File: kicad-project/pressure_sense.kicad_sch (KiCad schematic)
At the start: 27 parts

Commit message: cleaning up footprints
used easyeda2kicad.py to get better footprints (with 3d models) (https://github.com/uPesy/easyeda2kicad.py)

it's kinda messy bc some symbols are kicad and others easyeda, shouldn't matter tho (e.g. on C6 can't see the 470u value, only part ref)
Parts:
- removed C6: 470u, 470uF:CAP-SMD_BD6.3-L6.6-W6.6-FD, symbol Device:C_Polarized
- removed H1: X6521WR-2×17H-C30D60, 2*17P:HDR-TH_34P-P2.54-H-M-R2-C17-S2.54, symbol 2*17P:X6521WR-2×17H-C30D60
- removed JL1, JR1: Conn_01x22_Socket, 22P:HDR-TH_22P-P2.54-V-M, symbol Connector:Conn_01x22_Socket
- removed JPWR1: Screw_Terminal_01x02, 2P:CONN-TH_P2.54_KF128-2.54-2P, symbol Connector:Screw_Terminal_01x02
- removed RV1: 20k, pot:RES-ADJ-TH_3P-L7.1-W6.9-P2.50-L_3362P, symbol Device:R_Potentiometer_Trim
- removed UA1, UB1: SN74HC163DR_C338758, SN74HC163DR:SOIC-16_L9.9-W3.9-P1.27-LS6.0-BL, symbol SN74HC163DR:SN74HC163DR_C338758
- removed UA2, UB2: CD74HC4067SM96, CD74HC4067SM96:SSOP-24_L8.1-W5.3-P0.65-LS7.8-BL, symbol CD74HC6946SM96:CD74HC4067SM96
- removed USBC1: TYPE-C-31-M-12, USBC:USB-C_SMD-TYPE-C-31-M-12_1, symbol USBC:TYPE-C-31-M-12
- added C6: UT1A471M0607VG, easyeda2kicad:CAP-SMD_BD6.3-L6.6-W6.6-FD, symbol easyeda2kicad:UT1A471M0607VG
- added H2, H3, H4: MountingHole, MountingHole:MountingHole_3.2mm_M3, symbol Mechanical:MountingHole
- added H5: X6521WR-2×17H-C30D60, easyeda2kicad:HDR-TH_34P-P2.54-H-M-R2-C17-S2.54, symbol easyeda2kicad:X6521WR-2×17H-C30D60
- added JL1, JR1: FH2.54-09-22PZD, easyeda2kicad:HDR-TH_22P-P2.54-V-M, symbol easyeda2kicad:FH2.54-09-22PZD
- added JPWR1: KF128-2.54-2P, easyeda2kicad:CONN-TH_P2.54_KF128-2.54-2P, symbol easyeda2kicad:KF128-2.54-2P
- added RV1: 3362P-1-203_C118933, easyeda2kicad:RES-ADJ-TH_3P-L7.1-W6.9-P2.50-L_3362P, symbol easyeda2kicad:3362P-1-203_C118933
- added UA1, UB1: SN74HC163DR_C338758, easyeda2kicad:SOIC-16_L9.9-W3.9-P1.27-LS6.0-BL, symbol easyeda2kicad:SN74HC163DR_C338758
- added UA2, UB2: CD74HC4067SM96, easyeda2kicad:SSOP-24_L8.1-W5.3-P0.65-LS7.8-BL, symbol easyeda2kicad:CD74HC4067SM96
- added USBC1: TYPE-C-31-M-12, easyeda2kicad:USB-C_SMD-TYPE-C-31-M-12_1, symbol easyeda2kicad:TYPE-C-31-M-12
- C1, C10, C2, C3, C7, C9: footprint 100nF:C0402 -> easyeda2kicad:C0402
- C4: footprint 100nF:C0402 -> easyeda2kicad:C0402; JLC_3DModel 32fe2cf9314f444ca2785a33c2db7189 -> (none); JLC_3D_Size 1 0.5 -> (none)
- C5: footprint 1000uF:CAP-SMD_BD10.0-L10.3-W10.3-LS11.3-FD -> easyeda2kicad:CAP-SMD_BD10.0-L10.3-W10.3-FD
- JA1, JB1: footprint IDC:IDC-TH_16P-P2.54_C3406 -> easyeda2kicad:IDC-TH_16P-P2.54_C3406
- JLED1: footprint 3P:CONN-TH_3P-P2.54_KF128-2.54-3P -> easyeda2kicad:CONN-TH_3P-P2.54_KF128-2.54-3P
- LED1: footprint _WS2812B-2020-V6:LED-SMD_4P-L2.2-W2.0-P1.00_WS2815C-2020-4P -> easyeda2kicad:LED-SMD_4P-L2.2-W2.0-P1.00_WS2815C-2020-4P
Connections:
- net +3.3V: now also H5.33, JL1.1, JL1.2, UA1.10 (ENT), UA1.16 (VCC), UA1.7 (ENP), UA1.9 (~{LOAD}), UA2.24 (VCC), UB1.10 (ENT), UB1.16 (VCC), UB1.9 (~{LOAD}), UB2.24 (VCC)
- net +5V: now also C4.2, C6.1, JL1.21, JPWR1.1, USBC1.A4B9 (VBUS), USBC1.B4A9 (VBUS); no longer C4.1
- net D0: now also H5.7, JR1.14
- net D1: now also H5.27, JR1.4
- net D10: now also H5.16, JL1.16
- net D11: now also H5.14, JL1.17
- net D12: now also H5.12, JL1.18
- net D13: now also H5.10, JL1.19
- net D14: now also H5.8, JL1.20
- net D15: now also H5.32, JL1.8
- net D16: now also H5.30, JL1.9
- net D17: now also H5.28, JL1.10
- net D18: now also H5.26, JL1.11
- net D19: now also H5.1, JR1.20
- net D2: now also H5.25, JR1.5
- net D20: now also H5.2, JR1.19
- net D21: now also H5.4, JR1.18
- net D3: now also H5.22, JL1.13
- net D35: now also H5.9, JR1.13
- net D36: now also H5.11, JR1.12
- net D37: now also H5.13, JR1.11
- net D38: now also H5.15, JR1.10
- net D39: now also H5.17, JR1.9
- net D4: now also JL1.4, RV1.2, UB2.1 (COMMONINOUT/OUTPUT)
- net D40: now also H5.19, JR1.8
- net D41: now also H5.21, JR1.7
- net D42: now also H5.23, JR1.6
- net D45: now also H5.5, JR1.15
- net D46: now also H5.20, JL1.14
- net D47: now also H5.6, JR1.17
- net D48: now also H5.3, JR1.16
- net D5: now also JL1.5
- net D6: now also JL1.6, UA1.2 (CLK), UB1.2 (CLK)
- net D7: now also JL1.7, UA1.1 (~{CLR}), UB1.1 (~{CLR})
- net D8: now also H5.24, JL1.12
- net D9: now also H5.18, JL1.15
- net GND: now also C4.1, C6.2, JL1.22, JPWR1.2, JR1.1, JR1.21, JR1.22, UA1.3 (A), UA1.4 (B), UA1.5 (C), UA1.6 (D), UA1.8 (GND), UA2.1 (COMMONINOUT/OUTPUT), UA2.12 (GND), UA2.15 (~{E}), UB1.3 (A), UB1.4 (B), UB1.5 (C), UB1.6 (D), UB1.8 (GND), UB2.12 (GND), UB2.15 (~{E}), USBC1.1 (EH), USBC1.2 (EH), USBC1.3 (EH), USBC1.4 (EH), USBC1.A1B12 (GND), USBC1.B1A12 (GND); no longer C4.2
- net I0A: now also UA2.9 (I0)
- net I0B: now also UB2.9 (I0)
- net I10A: now also UA2.21 (I10)
- net I10B: now also UB2.21 (I10)
- net I11A: now also UA2.20 (I11)
- net I11B: now also UB2.20 (I11)
- net I12A: now also UA2.19 (I12)
- net I12B: now also UB2.19 (I12)
- net I13A: now also UA2.18 (I13)
- net I13B: now also UB2.18 (I13)
- net I14A: now also UA2.17 (I14)
- net I14B: now also UB2.17 (I14)
- net I15A: now also UA2.16 (I15)
- net I15B: now also UB2.16 (I15)
- net I1A: now also UA2.8 (I1)
- net I1B: now also UB2.8 (I1)
- net I2A: now also UA2.7 (I2)
- net I2B: now also UB2.7 (I2)
- net I3A: now also UA2.6 (I3)
- net I3B: now also UB2.6 (I3)
- net I4A: now also UA2.5 (I4)
- net I4B: now also UB2.5 (I4)
- net I5A: now also UA2.4 (I5)
- net I5B: now also UB2.4 (I5)
- net I6A: now also UA2.3 (I6)
- net I6B: now also UB2.3 (I6)
- net I7A: now also UA2.2 (I7)
- net I7B: now also UB2.2 (I7)
- net I8A: now also UA2.23 (I8)
- net I8B: now also UB2.23 (I8)
- net I9A: now also UA2.22 (I9)
- net I9B: now also UB2.22 (I9)
- net QA1: now also UA1.14 (QA), UA2.11 (S1)
- net QA2: now also UB1.14 (QA), UB2.11 (S1)
- net QB1: now also UA1.13 (QB), UA2.10 (S0)
- net QB2: now also UB1.13 (QB), UB2.10 (S0)
- net QC1: now also UA1.12 (QC), UA2.14 (S2)
- net QC2: now also UB1.12 (QC), UB2.14 (S2)
- net QD1: now also UA1.11 (QD), UA2.13 (S3)
- net QD2: now also UB1.11 (QD), UB2.13 (S3)
- net RCO: now also UA1.15 (RCO), UB1.7 (ENP)
- net RST: now also H5.34, JL1.3
- net RX: now also H5.29, JR1.3
- net TX: now also H5.31, JR1.2
- net at R4.2: now also RV1.3
- net at R1.1: now also USBC1.A5 (CC1)
- net at R2.2: now also USBC1.B5 (CC2)
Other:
- moved on the sheet: R4

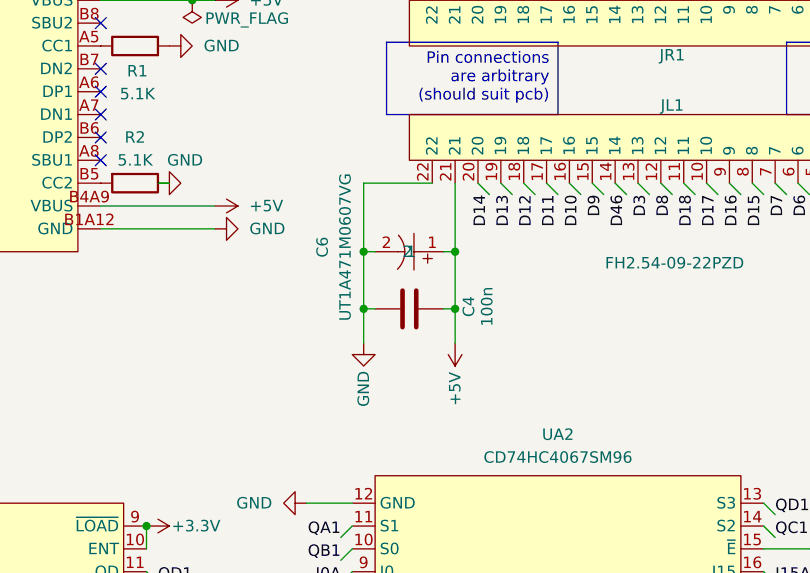
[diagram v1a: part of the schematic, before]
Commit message: changed capacitor for cost
the two smd caps cost extra $6 just for the toolhead! I changed it to one tht that is hand-soldered (the leads need to be bent)
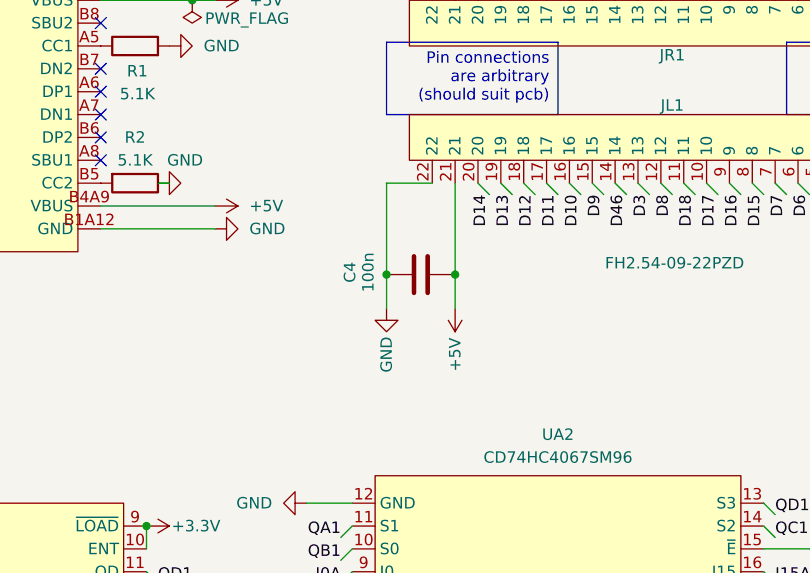
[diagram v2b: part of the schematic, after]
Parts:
- removed C6: UT1A471M0607VG, easyeda2kicad:CAP-SMD_BD6.3-L6.6-W6.6-FD, symbol easyeda2kicad:UT1A471M0607VG
- C5: footprint easyeda2kicad:CAP-SMD_BD10.0-L10.3-W10.3-FD -> easyeda2kicad:CAP-TH_BD10.0-P5.00-D0.6-FD
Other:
- moved on the sheet: C4

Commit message: changed usbc port
the port had tiny pads, i changed it for a less dodgy 6p one cause I don't need data

dw I adjusted positions.csv
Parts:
- removed USBC1: TYPE-C-31-M-12, easyeda2kicad:USB-C_SMD-TYPE-C-31-M-12_1, symbol easyeda2kicad:TYPE-C-31-M-12
- added USB1: TYPE-C 6P, easyeda2kicad:TYPE-C-SMD_TYPE-C-6P_1, symbol easyeda2kicad:TYPE-C6P
- C1, C10, C2, C3, C4, C7, C9: LCSC Part (none) -> C1525; LCSC Part # C1525 -> (none)
- C5: footprint easyeda2kicad:CAP-TH_BD10.0-P5.00-D0.6-FD -> footprints:cap_flat; LCSC Part (none) -> C439782; LCSC Part # C3359 -> (none)
- H2, H3, H4: LCSC Part (none) -> C725929
- H5: LCSC Part (none) -> C3406; LCSC Part # C725929 -> (none)
- JA1, JB1: LCSC Part (none) -> C7500786; LCSC Part # C3406 -> (none)
- JL1, JR1: LCSC Part (none) -> C474921; LCSC Part # C7500786 -> (none)
- JLED1: LCSC Part (none) -> C474920; LCSC Part # C474921 -> (none)
- JPWR1: LCSC Part (none) -> C52917434; LCSC Part # C474920 -> (none)
- LED1: LCSC Part (none) -> C25905; LCSC Part # C52917434 -> (none)
- R1, R2: LCSC Part (none) -> C25104; LCSC Part # C25905 -> (none)
- R3: LCSC Part (none) -> C25890; LCSC Part # C25104 -> (none)
- R4: LCSC Part (none) -> C118933; LCSC Part # C25890 -> (none)
- RV1: LCSC Part (none) -> C338758; LCSC Part # C118933 -> (none)
- UA1, UB1: LCSC Part (none) -> C98457; LCSC Part # C338758 -> (none)
- UA2, UB2: LCSC Part (none) -> C1525; LCSC Part # C98457 -> (none)
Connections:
- net +5V: now also USB1.A9 (VBUS), USB1.B9 (VBUS)
- net GND: now also USB1.7 (EH), USB1.A12 (GND), USB1.B12 (GND); no longer JR1.1
- net at R1.1: now also USB1.A5 (CC1)
- net at R2.2: now also USB1.B5 (CC2)
- no-connect marks 8 -> 3

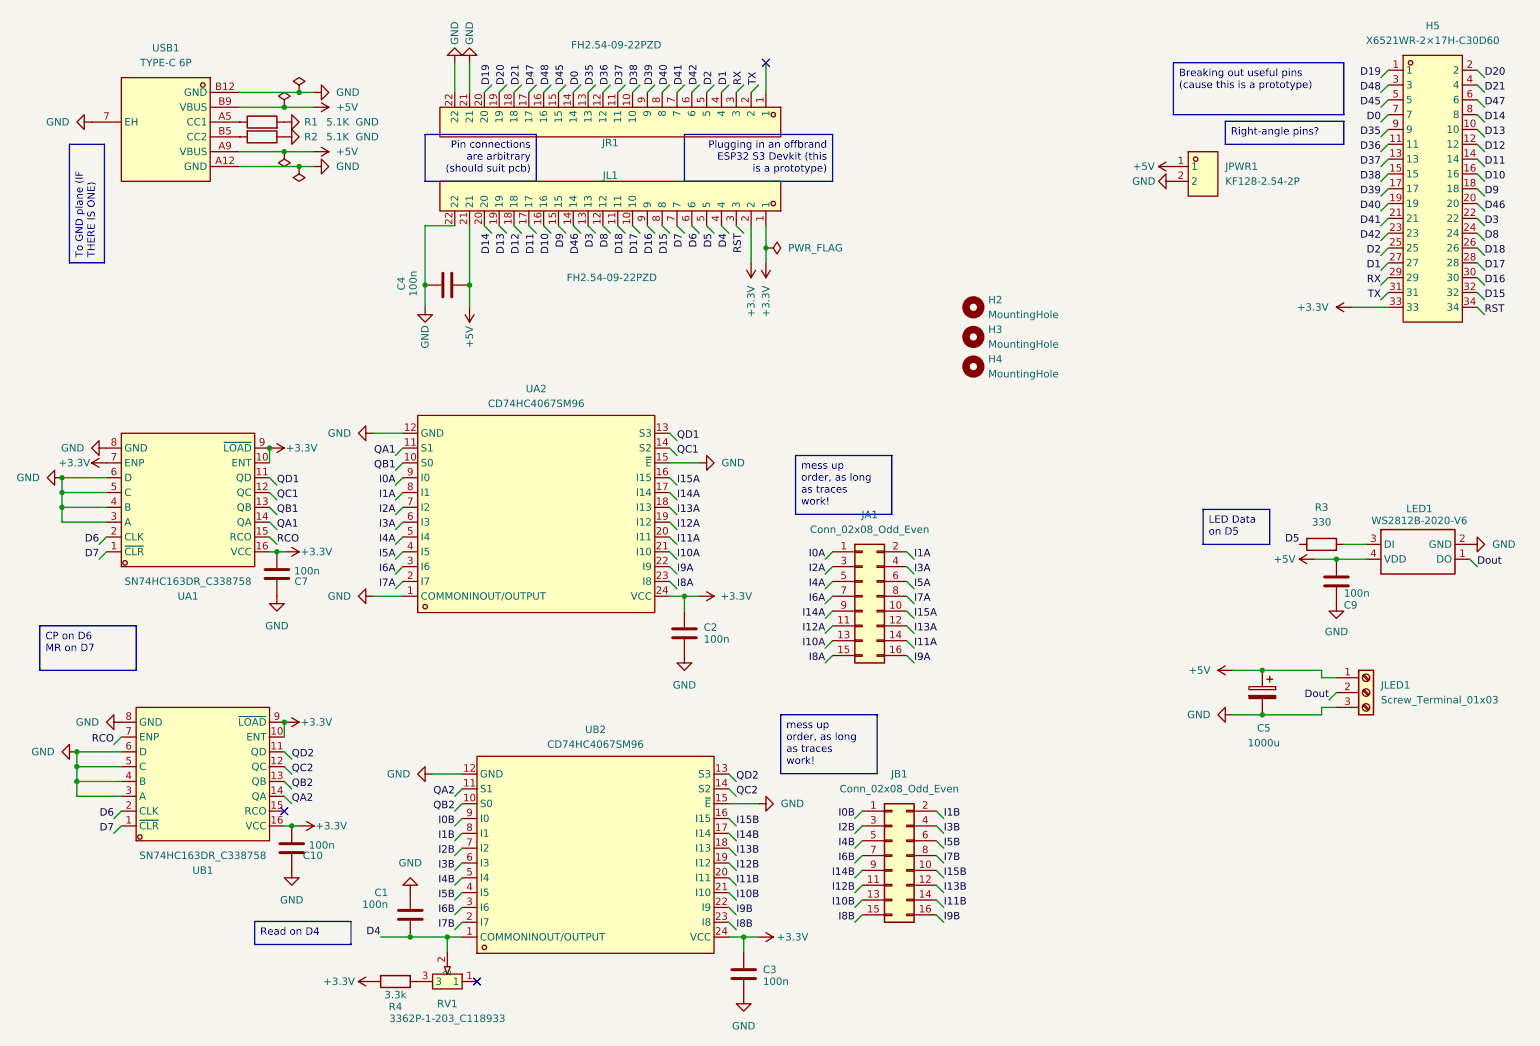
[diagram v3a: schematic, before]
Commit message: BIG CHANGE TO PCB
So since there's actually more time on Fallout, I decided to make the schematic simpler (so it's cheaper and smaller) by removing the uneccesary 74hc163 counters (there's plenty of gpio!)
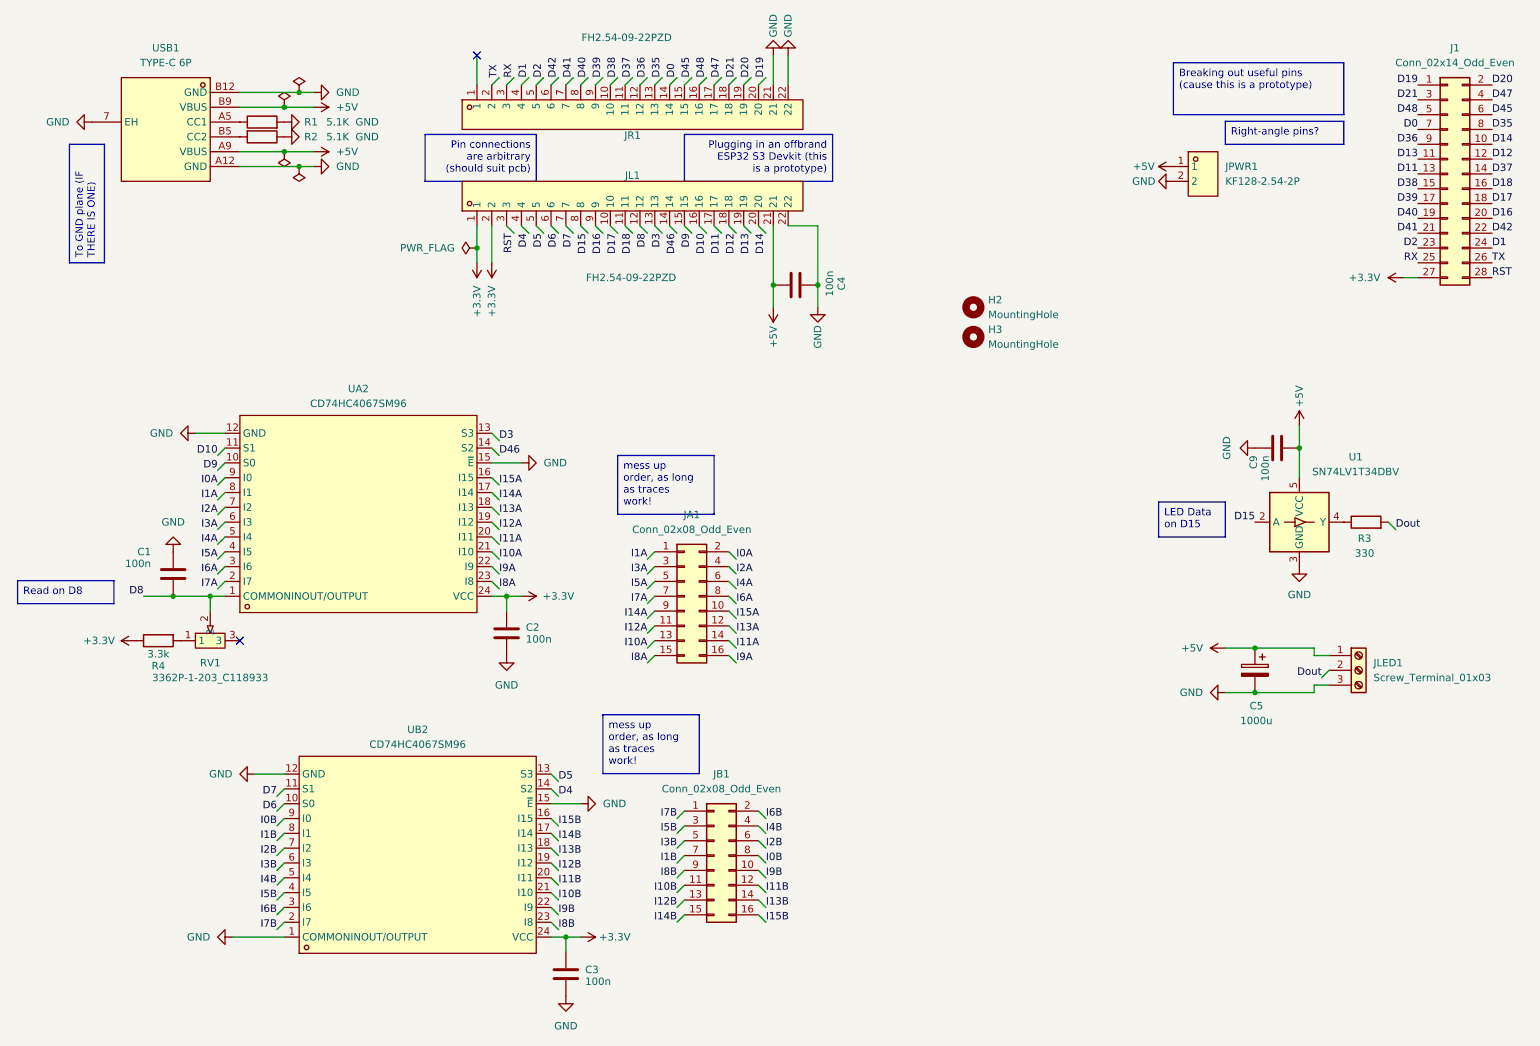
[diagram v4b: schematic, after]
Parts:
- removed C10, C7: 100n, easyeda2kicad:C0402, symbol Device:C
- removed H4: MountingHole, MountingHole:MountingHole_3.2mm_M3, symbol Mechanical:MountingHole
- removed H5: X6521WR-2×17H-C30D60, easyeda2kicad:HDR-TH_34P-P2.54-H-M-R2-C17-S2.54, symbol easyeda2kicad:X6521WR-2×17H-C30D60
- removed LED1: WS2812B-2020-V6, easyeda2kicad:LED-SMD_4P-L2.2-W2.0-P1.00_WS2815C-2020-4P, symbol _WS2812B-2020-V6:WS2812B-2020-V6
- removed UA1, UB1: SN74HC163DR_C338758, easyeda2kicad:SOIC-16_L9.9-W3.9-P1.27-LS6.0-BL, symbol easyeda2kicad:SN74HC163DR_C338758
- added J1: Conn_02x14_Odd_Even, easyeda2kicad:HDR-TH_28P-P2.54-H-M-R2-C14-S2.54, symbol Connector_Generic:Conn_02x14_Odd_Even
- added U1: SN74LV1T34DBV, Package_TO_SOT_SMD:SOT-23-5_HandSoldering, symbol Logic_LevelTranslator:SN74LV1T34DBV
- C1, C2, C3, C4, C9: footprint easyeda2kicad:C0402 -> Capacitor_SMD:C_0805_2012Metric_Pad1.18x1.45mm_HandSolder; LCSC Part C1525 -> C28233
- R1, R2: footprint Resistor_SMD:R_0402_1005Metric -> Resistor_SMD:R_0805_2012Metric_Pad1.20x1.40mm_HandSolder; LCSC Part C25104 -> C27834
- R3: footprint Resistor_SMD:R_0402_1005Metric -> Resistor_SMD:R_0805_2012Metric_Pad1.20x1.40mm_HandSolder; LCSC Part C25890 -> C17630
- R4: footprint Resistor_SMD:R_0402_1005Metric -> Resistor_SMD:R_0805_2012Metric_Pad1.20x1.40mm_HandSolder; LCSC Part C118933 -> C26020
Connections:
- net QA1 is gone; now on net D10: UA2.11 (S1)
- net QA2 is gone; now on net D7: UB2.11 (S1)
- net QB1 is gone; now on net D9: UA2.10 (S0)
- net QB2 is gone; now on net D6: UB2.10 (S0)
- net QC1 is gone; now on net D46: UA2.14 (S2)
- net QC2 is gone; now on net D4: UB2.14 (S2)
- net QD1 is gone; now on net D3: UA2.13 (S3)
- net QD2 is gone; now on net D5: UB2.13 (S3)
- net +3.3V: now also J1.27 (Pin_27)
- net +5V: now also U1.5 (VCC)
- net D0: now also J1.7 (Pin_7)
- net D1: now also J1.24 (Pin_24)
- net D11: now also J1.13 (Pin_13)
- net D12: now also J1.12 (Pin_12)
- net D13: now also J1.11 (Pin_11)
- net D14: now also J1.10 (Pin_10)
- net D15: now also U1.2 (A)
- net D16: now also J1.20 (Pin_20)
- net D17: now also J1.18 (Pin_18)
- net D18: now also J1.16 (Pin_16)
- net D19: now also J1.1 (Pin_1)
- net D2: now also J1.23 (Pin_23)
- net D20: now also J1.2 (Pin_2)
- net D21: now also J1.3 (Pin_3)
- net D35: now also J1.8 (Pin_8)
- net D36: now also J1.9 (Pin_9)
- net D37: now also J1.14 (Pin_14)
- net D38: now also J1.15 (Pin_15)
- net D39: now also J1.17 (Pin_17)
- net D4: no longer C1.1, RV1.2, UB2.1 (COMMONINOUT/OUTPUT)
- net D40: now also J1.19 (Pin_19)
- net D41: now also J1.21 (Pin_21)
- net D42: now also J1.22 (Pin_22)
- net D45: now also J1.6 (Pin_6)
- net D47: now also J1.4 (Pin_4)
- net D48: now also J1.5 (Pin_5)
- net D5: no longer R3.1
- net D8: now also C1.1, RV1.2, UA2.1 (COMMONINOUT/OUTPUT)
- net Dout: now also R3.2
- net GND: now also UB2.1 (COMMONINOUT/OUTPUT), U1.3 (GND); no longer UA2.1 (COMMONINOUT/OUTPUT)
- net I0A: now also JA1.2 (Pin_2); no longer JA1.1 (Pin_1)
- net I0B: now also JB1.8 (Pin_8); no longer JB1.1 (Pin_1)
- net I10B: now also JB1.11 (Pin_11); no longer JB1.13 (Pin_13)
- net I11B: now also JB1.12 (Pin_12); no longer JB1.14 (Pin_14)
- net I12B: now also JB1.13 (Pin_13); no longer JB1.11 (Pin_11)
- net I13B: now also JB1.14 (Pin_14); no longer JB1.12 (Pin_12)
- net I14B: now also JB1.15 (Pin_15); no longer JB1.9 (Pin_9)
- net I15B: now also JB1.16 (Pin_16); no longer JB1.10 (Pin_10)
- net I1A: now also JA1.1 (Pin_1); no longer JA1.2 (Pin_2)
- net I1B: now also JB1.7 (Pin_7); no longer JB1.2 (Pin_2)
- net I2A: now also JA1.4 (Pin_4); no longer JA1.3 (Pin_3)
- net I2B: now also JB1.6 (Pin_6); no longer JB1.3 (Pin_3)
- net I3A: now also JA1.3 (Pin_3); no longer JA1.4 (Pin_4)
- net I3B: now also JB1.5 (Pin_5); no longer JB1.4 (Pin_4)
- net I4A: now also JA1.6 (Pin_6); no longer JA1.5 (Pin_5)
- net I4B: now also JB1.4 (Pin_4); no longer JB1.5 (Pin_5)
- net I5A: now also JA1.5 (Pin_5); no longer JA1.6 (Pin_6)
- net I5B: now also JB1.3 (Pin_3); no longer JB1.6 (Pin_6)
- net I6A: now also JA1.8 (Pin_8); no longer JA1.7 (Pin_7)
- net I6B: now also JB1.2 (Pin_2); no longer JB1.7 (Pin_7)
- net I7A: now also JA1.7 (Pin_7); no longer JA1.8 (Pin_8)
- net I7B: now also JB1.1 (Pin_1); no longer JB1.8 (Pin_8)
- net I8B: now also JB1.9 (Pin_9); no longer JB1.15 (Pin_15)
- net I9B: now also JB1.10 (Pin_10); no longer JB1.16 (Pin_16)
- net RST: now also J1.28 (Pin_28)
- net RX: now also J1.25 (Pin_25)
- net TX: now also J1.26 (Pin_26)
- net at RV1.1: now also R4.2
- net at RV1.3: no longer R4.2
- new net: R3.1, U1.4 (Y)
- no-connect marks 3 -> 2
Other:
- moved on the sheet: C2, C3, C4, C5, C9, JA1, JB1, JL1, JLED1, JR1, R3, UA2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
